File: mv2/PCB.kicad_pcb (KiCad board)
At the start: 2 copper layers, 70 x 90 mm, 41 parts, among them J1 SWD, J3 USB_C_Receptacle_USB2.0, SW1 SW_Push, U2 USBLC6-2SC6, U3 W25Q128JVS, Y1 12MHz

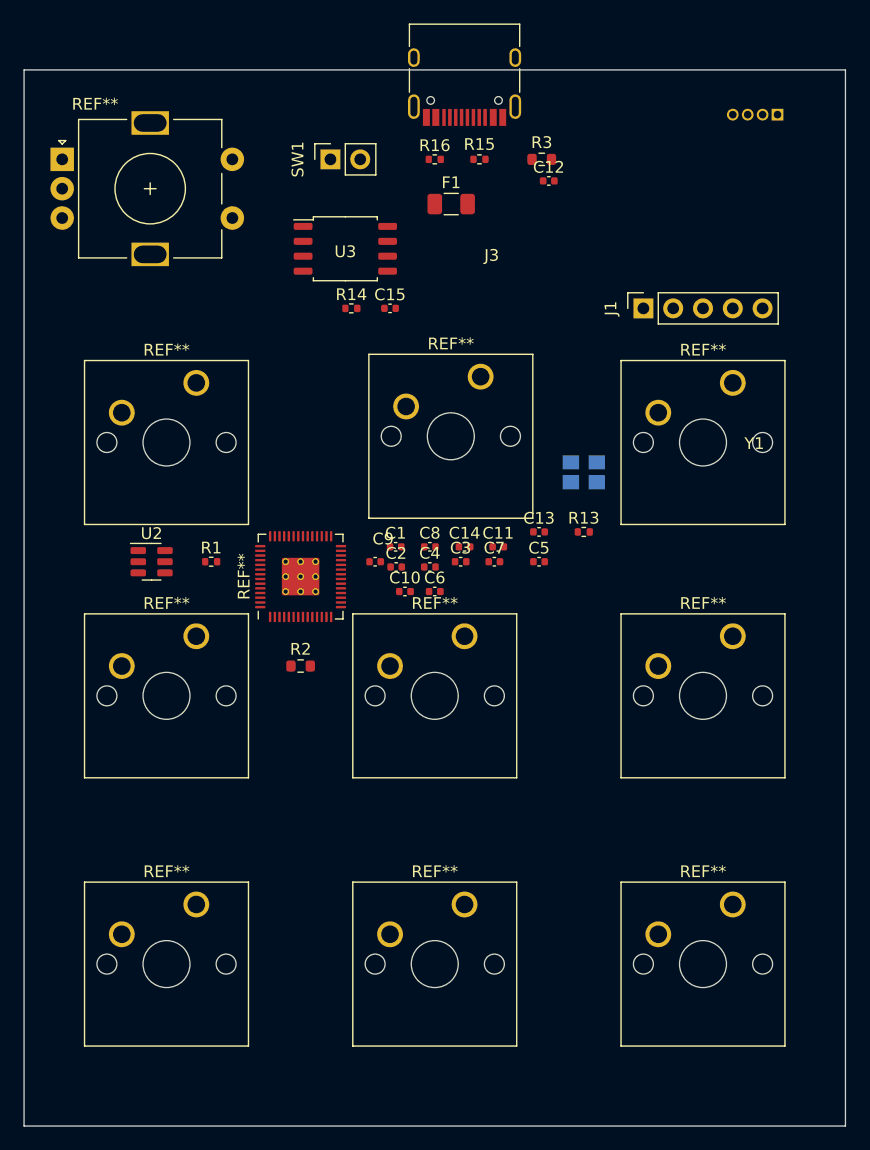
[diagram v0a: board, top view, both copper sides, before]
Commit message: pcb routed
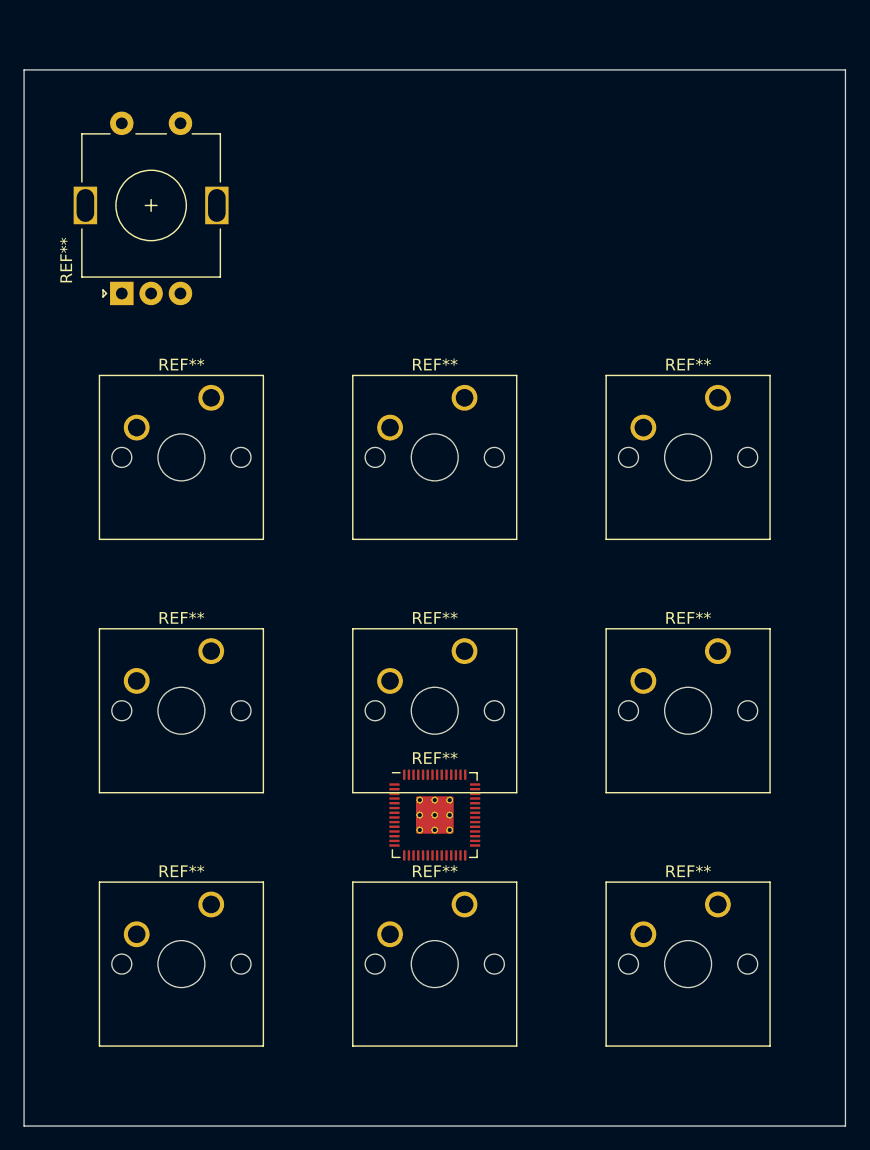
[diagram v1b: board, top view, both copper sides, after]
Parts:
- removed C1, C7: 1uF, Capacitor_SMD:C_0402_1005Metric
- removed C10, C11, C12, C13, C14, C15, C2, C3, C8, C9: 100nF, Capacitor_SMD:C_0402_1005Metric
- removed C4, C5: 22pF, Capacitor_SMD:C_0402_1005Metric
- removed C6: 10uF, Capacitor_SMD:C_0402_1005Metric
- removed F1: 500mA, Fuse:Fuse_1206_3216Metric
- removed J1: SWD, Connector_PinSocket_2.54mm:PinSocket_1x05_P2.54mm_Vertical
- removed J3: USB_C_Receptacle_USB2.0, Connector_USB:USB_C_Receptacle_HRO_TYPE-C-31-M-12
- removed R1, R13, R14: 1k, Resistor_SMD:R_0402_1005Metric
- removed R15, R16: 5k1, Resistor_SMD:R_0402_1005Metric
- removed R2, R3: 27R, Resistor_SMD:R_0603_1608Metric
- removed the REF** at (148.7, 89.6)
- removed the REF** at (174.0, 67.3)
- removed the REF** at (124.5, 90.2)
- removed the REF** at (170.2, 90.2)
- removed the REF** at (170.2, 134.6)
- removed the REF** at (124.5, 111.8)
- removed the REF** at (147.3, 111.8)
- removed the REF** at (170.2, 111.8)
- removed SW1: SW_Push, Connector_PinSocket_2.54mm:PinSocket_1x02_P2.54mm_Vertical
- removed U2: USBLC6-2SC6, Package_TO_SOT_SMD:SOT-23-6
- removed U3: W25Q128JVS, Package_SO:SOIC-8_5.23x5.23mm_P1.27mm
- removed Y1: 12MHz, Crystal:Crystal_SMD_3225-4Pin_3.2x2.5mm
- added REF**: SW_Cherry_MX_1.00u_PCB, Button_Switch_Keyboard:SW_Cherry_MX_1.00u_PCB, F.Cu at (168.9, 91.4)
- added REF**: SW_Cherry_MX_1.00u_PCB, Button_Switch_Keyboard:SW_Cherry_MX_1.00u_PCB, F.Cu at (168.9, 134.6)
- added REF**: SW_Cherry_MX_1.00u_PCB, Button_Switch_Keyboard:SW_Cherry_MX_1.00u_PCB, F.Cu at (125.7, 91.4)
- added REF**: SW_Cherry_MX_1.00u_PCB, Button_Switch_Keyboard:SW_Cherry_MX_1.00u_PCB, F.Cu at (168.9, 113.0)
- added REF**: SW_Cherry_MX_1.00u_PCB, Button_Switch_Keyboard:SW_Cherry_MX_1.00u_PCB, F.Cu at (147.3, 113.0)
- added REF**: SW_Cherry_MX_1.00u_PCB, Button_Switch_Keyboard:SW_Cherry_MX_1.00u_PCB, F.Cu at (125.7, 113.0)
- added REF**: SW_Cherry_MX_1.00u_PCB, Button_Switch_Keyboard:SW_Cherry_MX_1.00u_PCB, F.Cu at (147.3, 91.4)
- REF**: value RotaryEncoder_Alps_EC11E-Switch_Vertical_H20mm -> RotaryEncoder
- moved REF** 23.3 mm to (144.8, 127.0), turned to 0 degrees
- moved REF** 12.5 mm to (118.1, 82.5), turned to 90 degrees
- moved REF** 1.27 mm to (125.7, 134.6)
